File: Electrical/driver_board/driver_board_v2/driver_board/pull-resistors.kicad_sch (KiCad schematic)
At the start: 18 parts

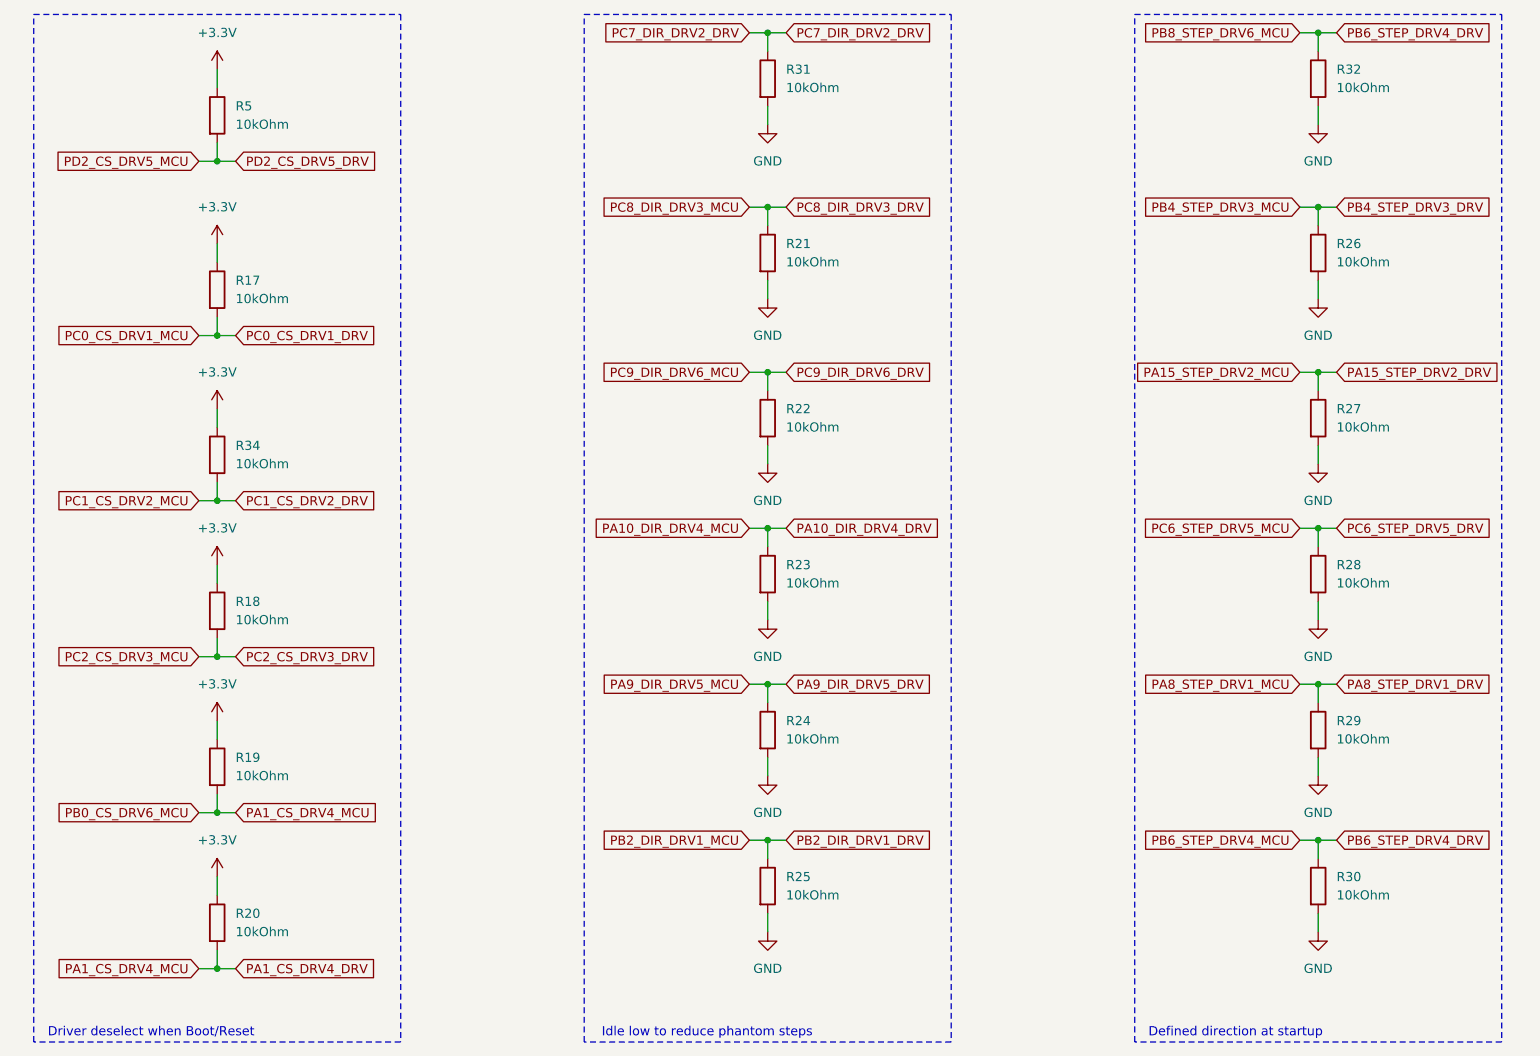
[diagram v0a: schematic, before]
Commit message: Assigned Pull up/downs
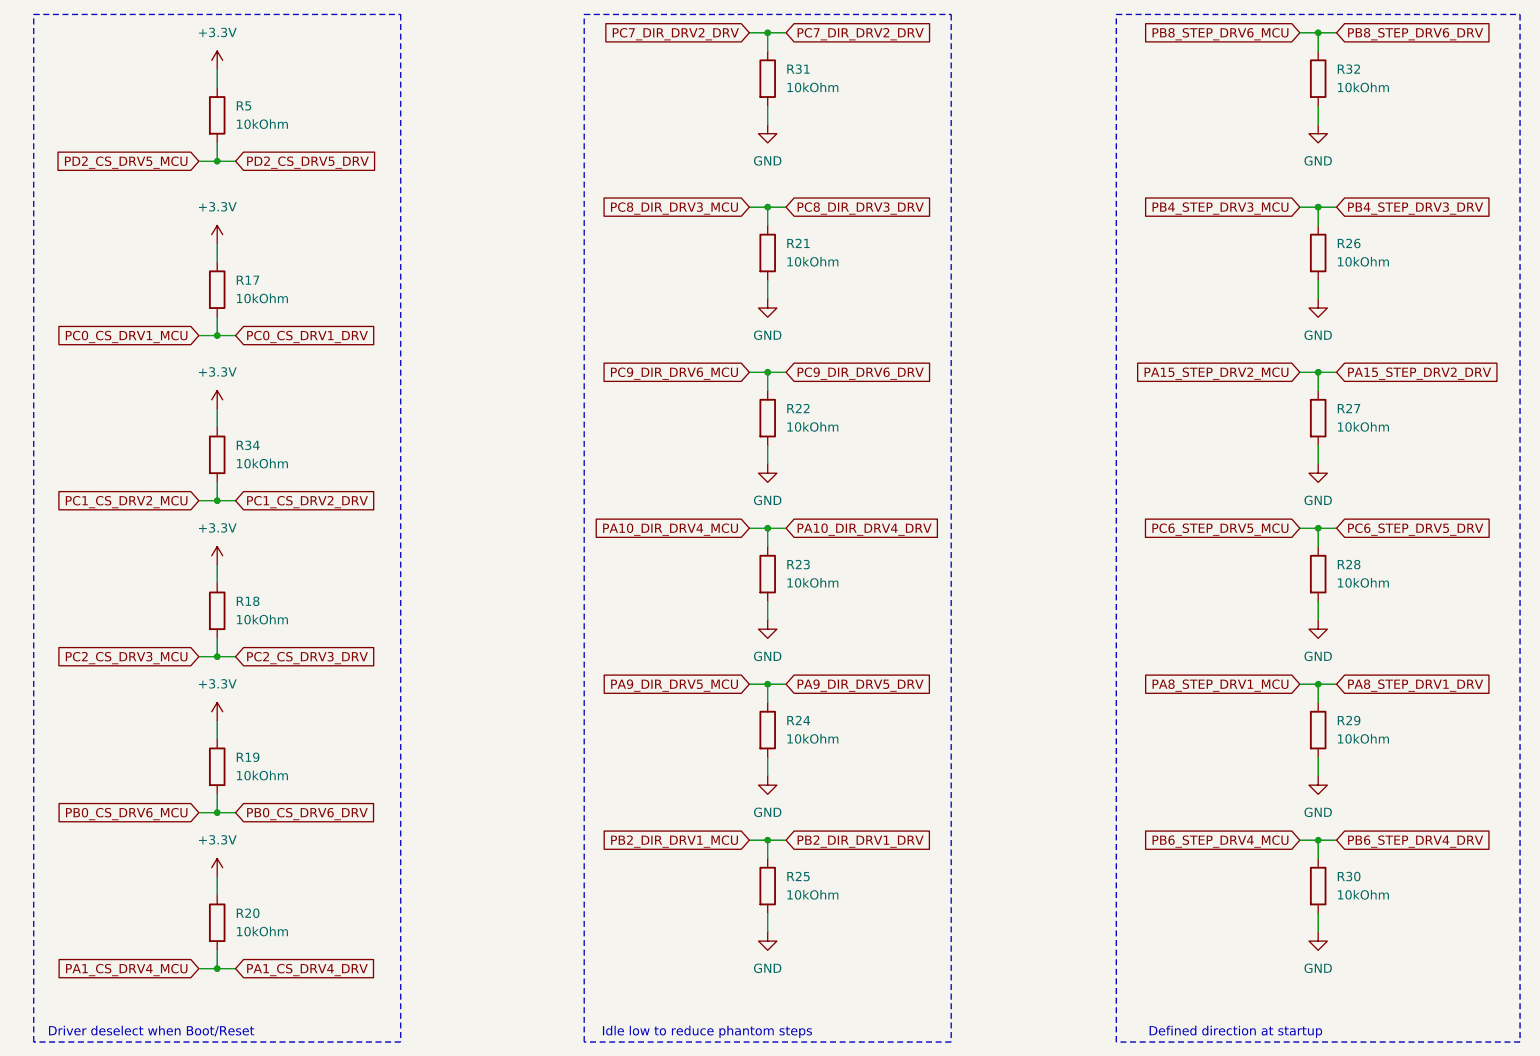
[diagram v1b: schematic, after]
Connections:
- net PA1_CS_DRV4_DRV: no longer R19.2
- net PB6_STEP_DRV4_DRV: no longer R32.1
- new net PB0_CS_DRV6_DRV: R19.2
- new net PB8_STEP_DRV6_DRV: R32.1

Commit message: Added new converter
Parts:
- renumbered R5 to R14, R17 to R15, R34 to R16, R18 to R17, R19 to R18, R20 to R19, R31 to R20, R32 to R26, R26 to R27, R27 to R28, R28 to R29, R29 to R30, R30 to R31
